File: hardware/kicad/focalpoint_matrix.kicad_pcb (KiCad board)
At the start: 2 copper layers, 128 x 128 mm, 33 parts

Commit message: align Rev A with sixteen dynamic controls
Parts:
- removed D14, D15, D16: , ComboDiode
- removed S14, S15, S16: , MX
- moved D13 30.0 mm to (30.0, -55.0)
- moved S13 30.0 mm to (30.0, -60.0)
- moved D12 2.00 mm to (60.0, -35.0)
- moved D3 2.00 mm to (0.00, -35.0)
- moved D6 2.00 mm to (20.0, -35.0)
- moved D9 2.00 mm to (40.0, -35.0)
- moved ROT1 2.00 mm to (60.0, 20.0)
- moved S12 2.00 mm to (60.0, -40.0)
- moved S3 2.00 mm to (0.00, -40.0)
- moved S6 2.00 mm to (20.0, -40.0)
- moved S9 2.00 mm to (40.0, -40.0)
- moved D11 1.00 mm to (60.0, -15.0)
- moved D2 1.00 mm to (0.00, -15.0)
- moved D5 1.00 mm to (20.0, -15.0)
- moved D8 1.00 mm to (40.0, -15.0)
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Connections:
- net accept_action renamed center_command

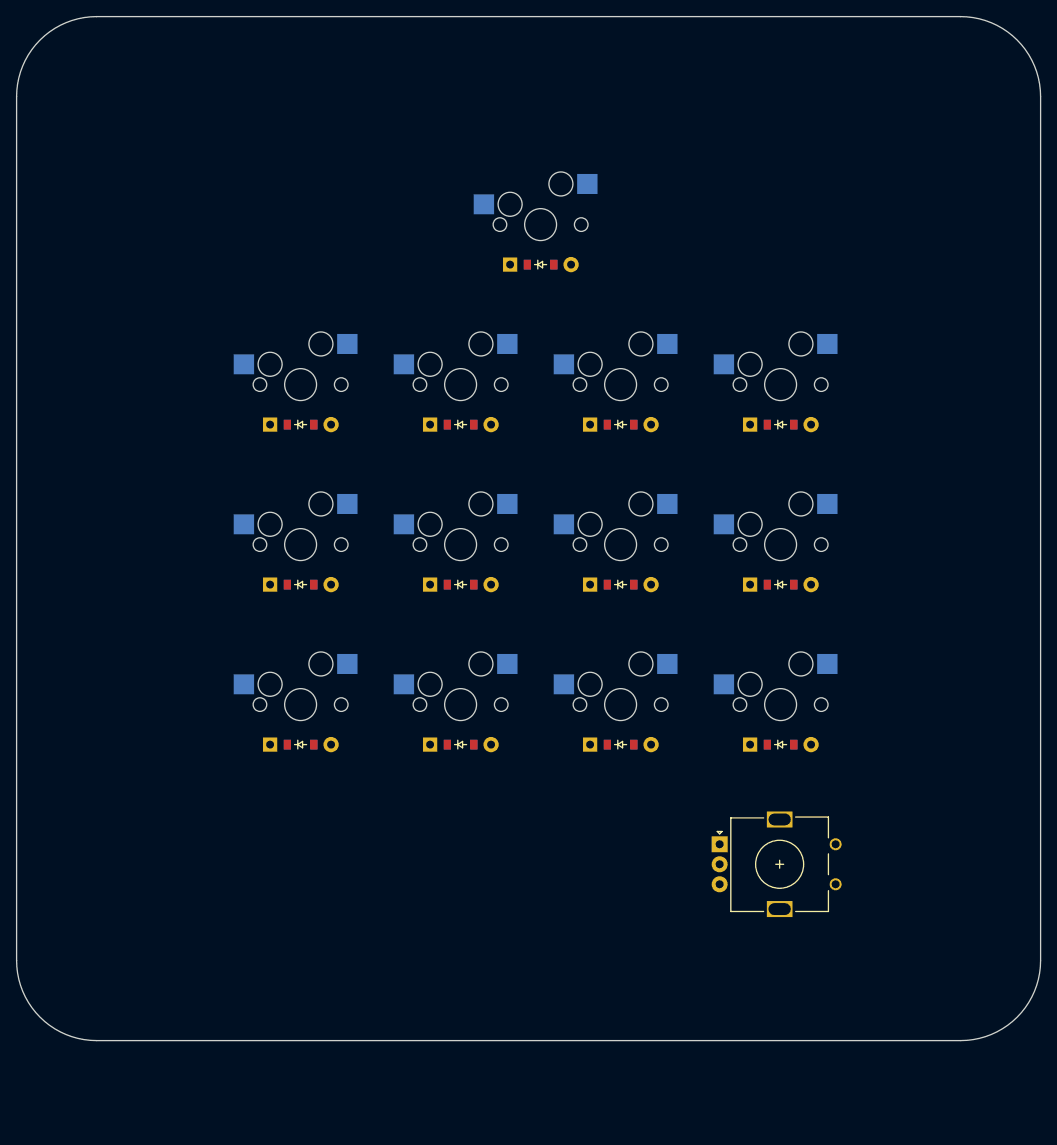
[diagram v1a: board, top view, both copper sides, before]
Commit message: arrange controls on uniform four by four grid
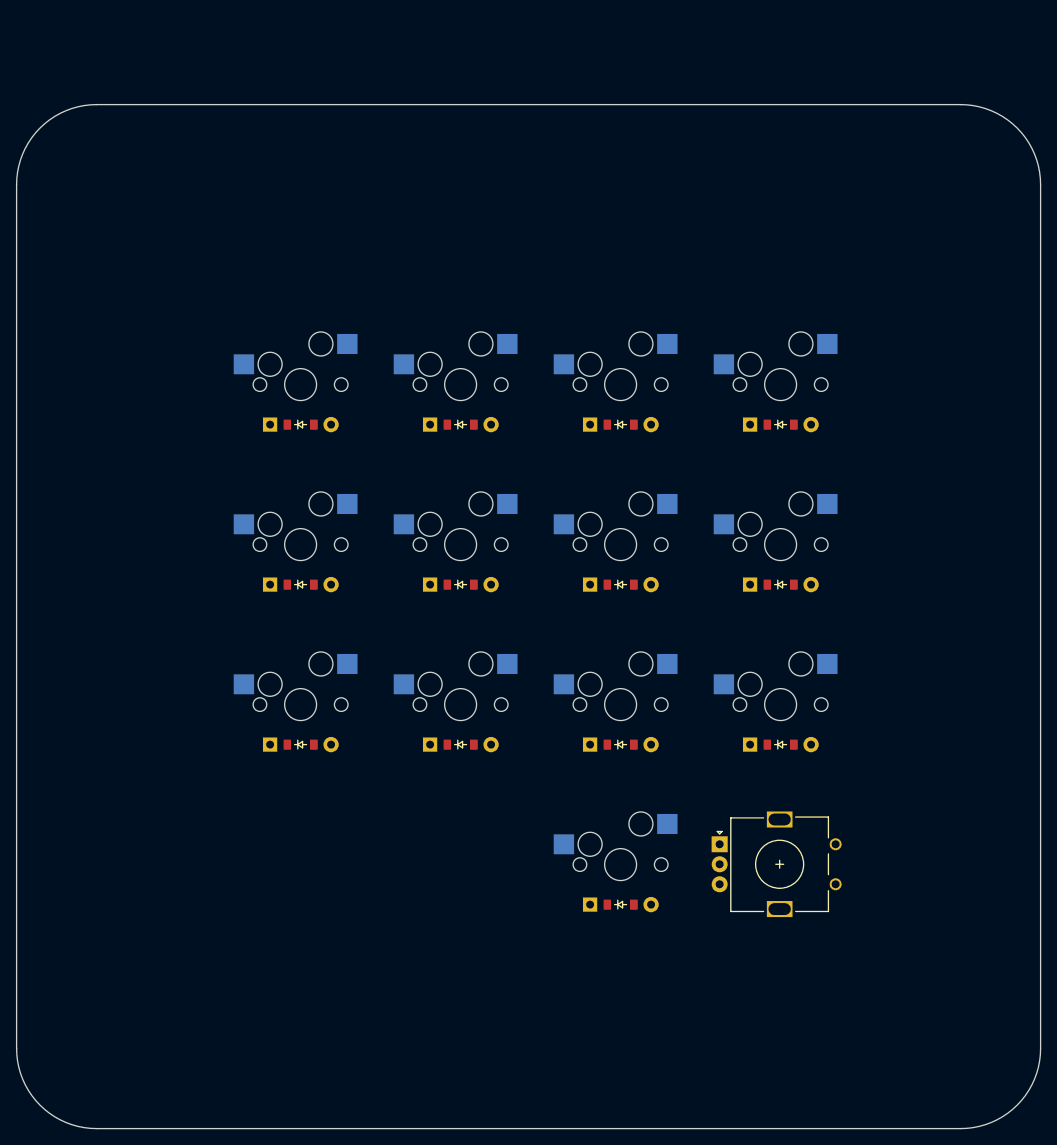
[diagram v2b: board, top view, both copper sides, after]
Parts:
- moved D13 80.6 mm to (40.0, 25.0)
- moved S13 80.6 mm to (40.0, 20.0)
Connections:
- net center_command renamed top_command
- S13 pad 2: C0 -> C2
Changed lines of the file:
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@@
 (net 15 "slot_4_row_2")
 (net 16 "slot_4_row_3")
-(net 17 "center_command")
+(net 17 "top_command")
 (net 18 "R0")
 (net 19 "R1")
@@
         )
       (module MX (layer F.Cu)
-      (at 30 -60 0)
+      (at 40 20 0)
       (fp_text reference "S13" (at 0 0) (layer F.SilkS) hide (effects (font (size 1.27 1.27) (thickness 0.15))))
       (fp_text value "" (at 0 0) (layer F.SilkS) hide (effects (font (size 1.27 1.27) (thickness 0.15))))
@@
         (pad "" np_thru_hole circle (at 2.54 -5.08) (size 3 3) (drill 3) (layers *.Cu *.Mask))
         (pad "" np_thru_hole circle (at -3.81 -2.54) (size 3 3) (drill 3) (layers *.Cu *.Mask))
-        (pad 1 smd rect (at -7.085 -2.54 0) (size 2.55 2.5) (layers B.Cu B.Paste B.Mask) (net 17 "center_command"))
-        (pad 2 smd rect (at 5.842 -5.08 0) (size 2.55 2.5) (layers B.Cu B.Paste B.Mask) (net 2 "C0"))
+        (pad 1 smd rect (at -7.085 -2.54 0) (size 2.55 2.5) (layers B.Cu B.Paste B.Mask) (net 17 "top_command"))
+        (pad 2 smd rect (at 5.842 -5.08 0) (size 2.55 2.5) (layers B.Cu B.Paste B.Mask) (net 10 "C2"))
         )
     (module ComboDiode (layer F.Cu)
@@
     )
     (module ComboDiode (layer F.Cu)
-        (at 30 -55 0)
+        (at 40 25 0)
         (fp_text reference "D13" (at 0 0) (layer F.SilkS) hide (effects (font (size 1.27 1.27) (thickness 0.15))))
         (fp_text value "" (at 0 0) (layer F.SilkS) hide (effects (font (size 1.27 1.27) (thickness 0.15))))
@@
         (fp_line (start -0.75 0) (end -0.35 0) (layer B.SilkS) (width 0.1))
         (pad 1 smd rect (at -1.65 0 0) (size 0.9 1.2) (layers F.Cu F.Paste F.Mask) (net 21 "R3"))
-        (pad 2 smd rect (at 1.65 0 0) (size 0.9 1.2) (layers B.Cu B.Paste B.Mask) (net 17 "center_command"))
+        (pad 2 smd rect (at 1.65 0 0) (size 0.9 1.2) (layers B.Cu B.Paste B.Mask) (net 17 "top_command"))
         (pad 1 smd rect (at -1.65 0 0) (size 0.9 1.2) (layers B.Cu B.Paste B.Mask) (net 21 "R3"))
-        (pad 2 smd rect (at 1.65 0 0) (size 0.9 1.2) (layers F.Cu F.Paste F.Mask) (net 17 "center_command"))
+        (pad 2 smd rect (at 1.65 0 0) (size 0.9 1.2) (layers F.Cu F.Paste F.Mask) (net 17 "top_command"))
         (pad 1 thru_hole rect (at -3.81 0 0) (size 1.778 1.778) (drill 0.9906) (layers *.Cu *.Mask) (net 21 "R3"))
-        (pad 2 thru_hole circle (at 3.81 0 0) (size 1.905 1.905) (drill 0.9906) (layers *.Cu *.Mask) (net 17 "center_command"))
+        (pad 2 thru_hole circle (at 3.81 0 0) (size 1.905 1.905) (drill 0.9906) (layers *.Cu *.Mask) (net 17 "top_command"))
     )
         (module rotary_encoder (layer F.Cu)
@@
             (pad "" thru_hole rect (at -0.12 5.56 0)  (size 3.2 2) (drill oval 2.8 1.5) (layers *.Cu *.Mask))
         )
-  (gr_line (start -25.5 42) (end 82.5 42) (layer Edge.Cuts) (stroke (width 0.15) (type default)))
-(gr_line (start 92.5 32) (end 92.5 -76) (layer Edge.Cuts) (stroke (width 0.15) (type default)))
-(gr_line (start 82.5 -86) (end -25.5 -86) (layer Edge.Cuts) (stroke (width 0.15) (type default)))
-(gr_line (start -35.5 -76) (end -35.5 32) (layer Edge.Cuts) (stroke (width 0.15) (type default)))
-(gr_arc (start 82.5 42) (mid 89.5710678 39.0710678) (end 92.5 32) (layer Edge.Cuts) (stroke (width 0.15) (type default)))
-(gr_arc (start 92.5 -76) (mid 89.5710678 -83.0710678) (end 82.5 -86) (layer Edge.Cuts) (stroke (width 0.15) (type default)))
-(gr_arc (start -25.5 -86) (mid -32.5710678 -83.0710678) (end -35.5 -76) (layer Edge.Cuts) (stroke (width 0.15) (type default)))
-(gr_arc (start -35.5 32) (mid -32.5710678 39.0710678) (end -25.5 42) (layer Edge.Cuts) (stroke (width 0.15) (type default)))
+  (gr_line (start -25.5 53) (end 82.5 53) (layer Edge.Cuts) (stroke (width 0.15) (type default)))
+(gr_line (start 92.5 43) (end 92.5 -65) (layer Edge.Cuts) (stroke (width 0.15) (type default)))
+(gr_line (start 82.5 -75) (end -25.5 -75) (layer Edge.Cuts) (stroke (width 0.15) (type default)))
+(gr_line (start -35.5 -65) (end -35.5 43) (layer Edge.Cuts) (stroke (width 0.15) (type default)))
+(gr_arc (start 82.5 53) (mid 89.5710678 50.0710678) (end 92.5 43) (layer Edge.Cuts) (stroke (width 0.15) (type default)))
+(gr_arc (start 92.5 -65) (mid 89.5710678 -72.0710678) (end 82.5 -75) (layer Edge.Cuts) (stroke (width 0.15) (type default)))
+(gr_arc (start -25.5 -75) (mid -32.5710678 -72.0710678) (end -35.5 -65) (layer Edge.Cuts) (stroke (width 0.15) (type default)))
+(gr_arc (start -35.5 43) (mid -32.5710678 50.0710678) (end -25.5 53) (layer Edge.Cuts) (stroke (width 0.15) (type default)))
 )

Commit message: place dial joystick and touch at matrix corners
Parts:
- moved D11 63.2 mm to (0.00, -35.0)
- moved D9 63.2 mm to (20.0, 25.0)
- moved S11 63.2 mm to (0.00, -40.0)
- moved S9 63.2 mm to (20.0, 20.0)
- moved D13 60.0 mm to (40.0, -35.0)
- moved ROT1 60.0 mm to (0.00, 20.0)
- moved S13 60.0 mm to (40.0, -40.0)
- moved D3 44.7 mm to (20.0, 5.00)
- moved S3 44.7 mm to (20.0, 0.00)
- moved D12 40.0 mm to (20.0, -35.0)
- moved S12 40.0 mm to (20.0, -40.0)
- moved D10 28.3 mm to (40.0, 25.0)
- moved D5 28.3 mm to (40.0, 5.00)
- moved D6 28.3 mm to (40.0, -15.0)
- moved S10 28.3 mm to (40.0, 20.0)
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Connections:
- net slot_1_row_1 renamed col_1_row_2
- net slot_1_row_2 renamed col_1_row_3
- net slot_1_row_3 renamed col_2_row_2
- net slot_2_row_1 renamed col_2_row_3
- net slot_2_row_2 renamed col_3_row_2
- net slot_2_row_3 renamed col_3_row_3
- net slot_3_row_1 renamed col_4_row_2
- net slot_3_row_2 renamed col_4_row_3
- net slot_3_row_3 renamed clear_row_1
- net slot_4_row_1 renamed ceramic_row_1
- net slot_4_row_2 renamed col_1_row_4
- net slot_4_row_3 renamed col_2_row_4
- net top_command renamed col_3_row_4
- D1 pad 1: R0 -> R1
- D11 pad 1: R1 -> R3
- D12 pad 1: R2 -> R3
- D2 pad 1: R1 -> R2
- D3 pad 1: R2 -> R1
- D4 pad 1: R0 -> R2
- D7 pad 1: R0 -> R1
- D8 pad 1: R1 -> R2
- D9 pad 1: R2 -> R0
- S10 pad 2: C3 -> C2
- S11 pad 2: C3 -> C0
- S12 pad 2: C3 -> C1
- S3 pad 2: C0 -> C1
- S5 pad 2: C1 -> C2
- S6 pad 2: C1 -> C2
- S7 pad 2: C2 -> C3
- S8 pad 2: C2 -> C3
- S9 pad 2: C2 -> C1

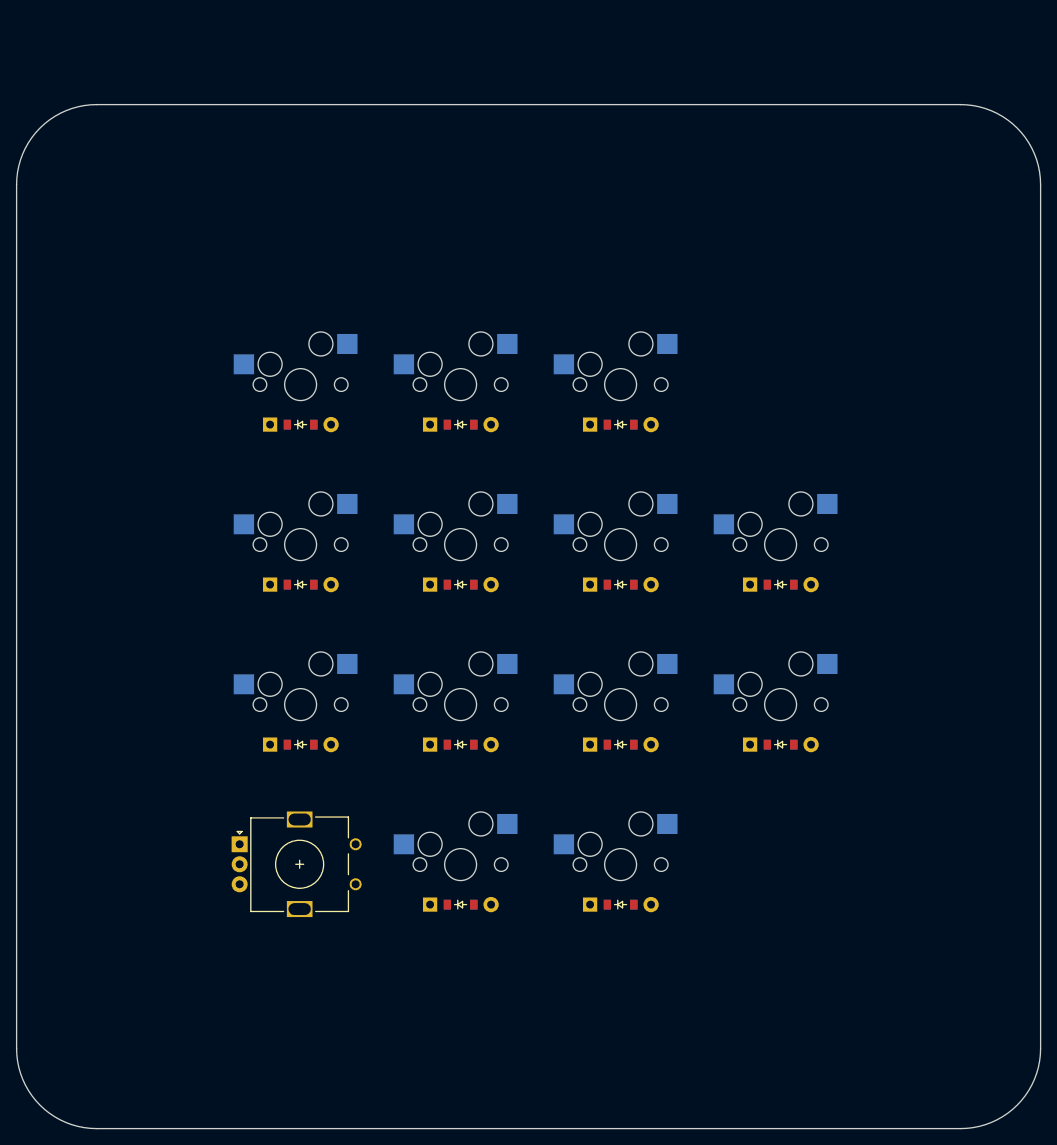
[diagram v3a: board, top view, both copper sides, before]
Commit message: tighten square enclosure around control grid
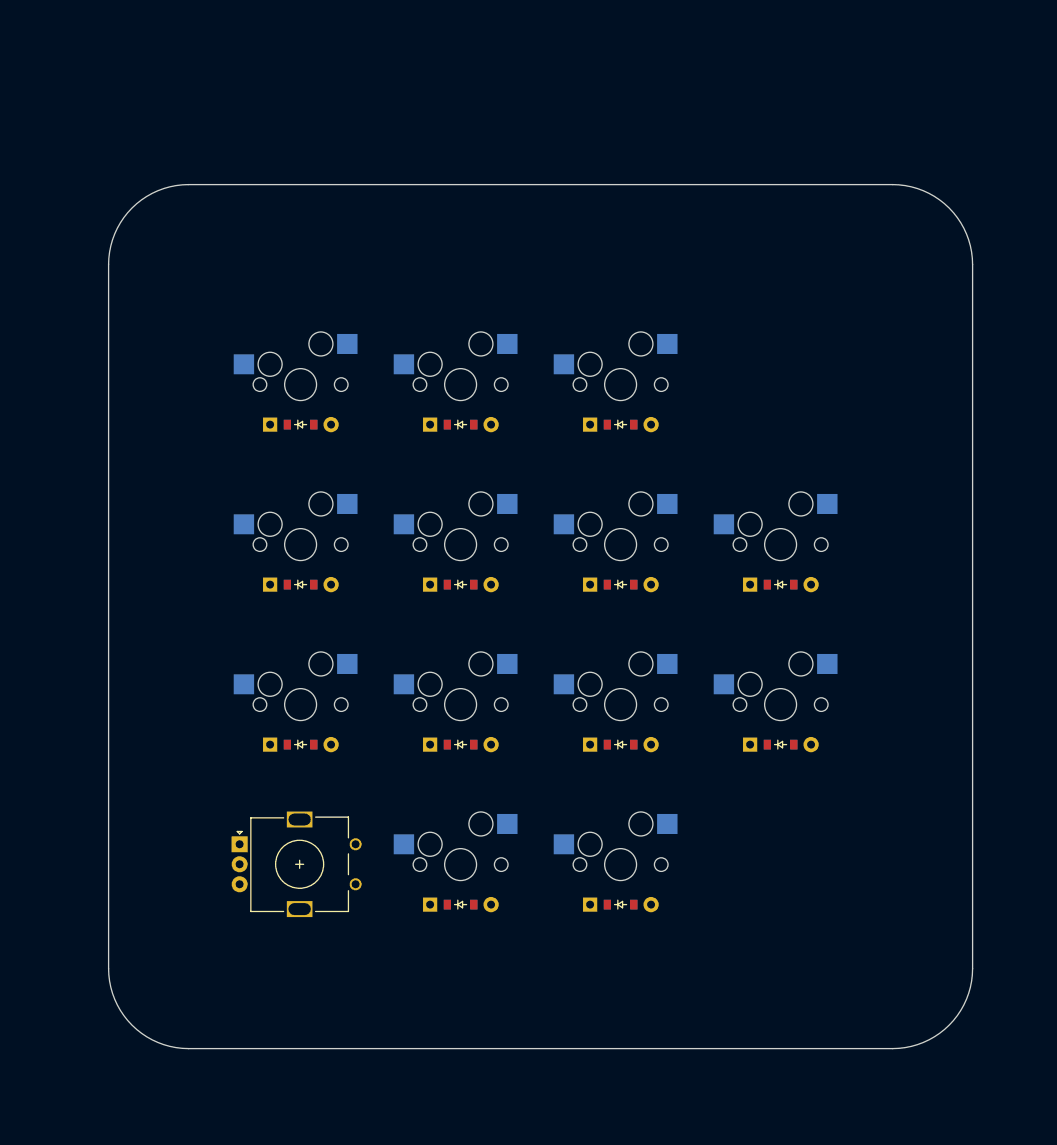
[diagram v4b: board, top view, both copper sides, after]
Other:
- board size 128 x 128 mm -> 108 x 108 mm
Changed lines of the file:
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@@
             (pad "" thru_hole rect (at -0.12 5.56 0)  (size 3.2 2) (drill oval 2.8 1.5) (layers *.Cu *.Mask))
         )
-  (gr_line (start -25.5 53) (end 82.5 53) (layer Edge.Cuts) (stroke (width 0.15) (type default)))
-(gr_line (start 92.5 43) (end 92.5 -65) (layer Edge.Cuts) (stroke (width 0.15) (type default)))
-(gr_line (start 82.5 -75) (end -25.5 -75) (layer Edge.Cuts) (stroke (width 0.15) (type default)))
-(gr_line (start -35.5 -65) (end -35.5 43) (layer Edge.Cuts) (stroke (width 0.15) (type default)))
-(gr_arc (start 82.5 53) (mid 89.5710678 50.0710678) (end 92.5 43) (layer Edge.Cuts) (stroke (width 0.15) (type default)))
-(gr_arc (start 92.5 -65) (mid 89.5710678 -72.0710678) (end 82.5 -75) (layer Edge.Cuts) (stroke (width 0.15) (type default)))
-(gr_arc (start -25.5 -75) (mid -32.5710678 -72.0710678) (end -35.5 -65) (layer Edge.Cuts) (stroke (width 0.15) (type default)))
-(gr_arc (start -35.5 43) (mid -32.5710678 50.0710678) (end -25.5 53) (layer Edge.Cuts) (stroke (width 0.15) (type default)))
+  (gr_line (start -14 43) (end 74 43) (layer Edge.Cuts) (stroke (width 0.15) (type default)))
+(gr_line (start 84 33) (end 84 -55) (layer Edge.Cuts) (stroke (width 0.15) (type default)))
+(gr_line (start 74 -65) (end -14 -65) (layer Edge.Cuts) (stroke (width 0.15) (type default)))
+(gr_line (start -24 -55) (end -24 33) (layer Edge.Cuts) (stroke (width 0.15) (type default)))
+(gr_arc (start 74 43) (mid 81.0710678 40.0710678) (end 84 33) (layer Edge.Cuts) (stroke (width 0.15) (type default)))
+(gr_arc (start 84 -55) (mid 81.0710678 -62.0710678) (end 74 -65) (layer Edge.Cuts) (stroke (width 0.15) (type default)))
+(gr_arc (start -14 -65) (mid -21.0710678 -62.0710678) (end -24 -55) (layer Edge.Cuts) (stroke (width 0.15) (type default)))
+(gr_arc (start -24 33) (mid -21.0710678 40.0710678) (end -14 43) (layer Edge.Cuts) (stroke (width 0.15) (type default)))
 )
